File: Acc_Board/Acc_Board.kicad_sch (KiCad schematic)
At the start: 33 parts, among them J1 1053091202, J2 1053091202, J3 1053091202, J4 1053091202, J5 1053091202, J6 1053091202, K1 Relay_SPST-NO, U1 ISO1050DUB, U2 NUCLEO-L432KC, U3 L7805CV, U4 PQDE6W-Q110-S5-H-D

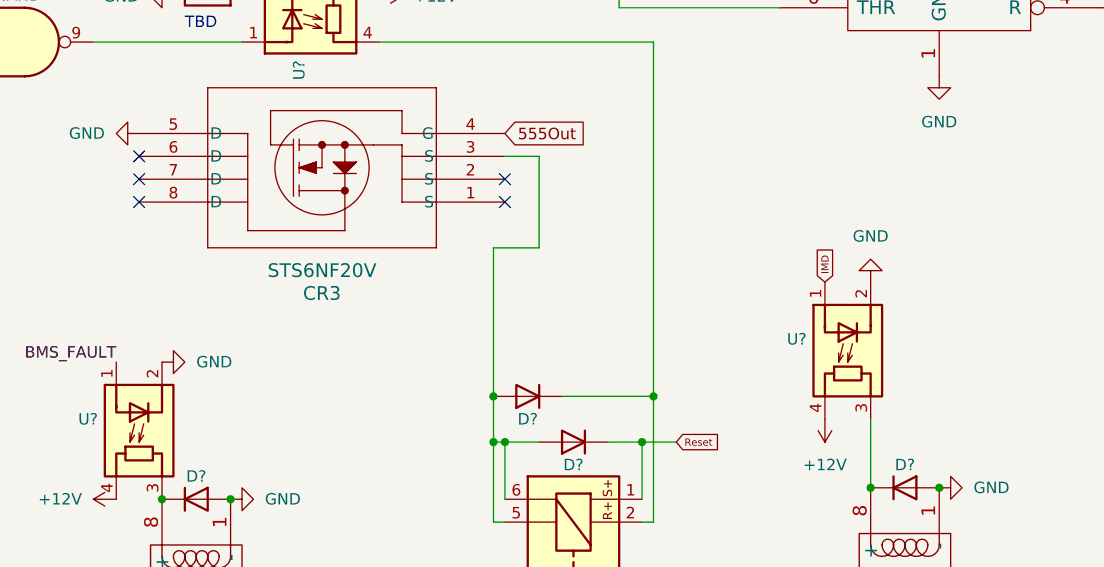
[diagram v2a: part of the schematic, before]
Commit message: Added resistors to optocouplers on ACC board
@goob10000 still needs to determine resistance
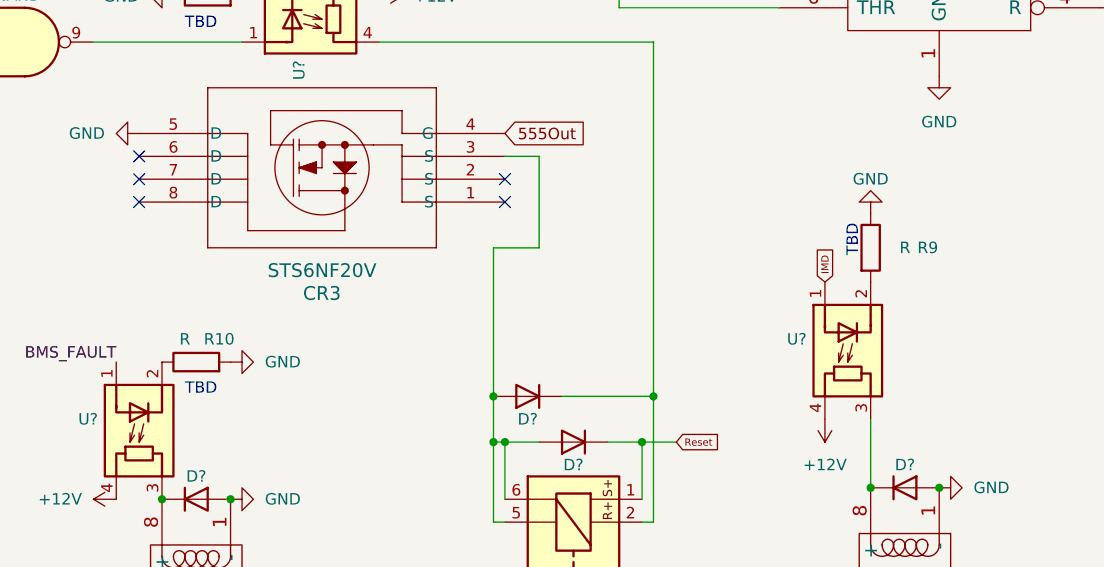
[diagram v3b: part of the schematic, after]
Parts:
- added R10, R9: R, symbol Device:R
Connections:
- net GND: now also R10.2, R9.1; no longer U?.2 (K), U?.2 (K)
- new net: R10.1, U?.2 (K)
- new net: R9.2, U?.2 (K)
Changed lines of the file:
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@@
     (effects (font (size 1.27 1.27)) (justify left bottom))
+  )
+  (text "TBD" (at 342.9 146.05 90)
+    (effects (font (size 1.27 1.27)) (justify right bottom))
   )
   (text "make cap smaller, resistor bigger\ncheck if 5V works; connect to DCDC"
@@
   )
   (text "Precharge Circuit" (at 27.94 118.11 0)
+    (effects (font (size 1.27 1.27)) (justify left bottom))
+  )
+  (text "TBD" (at 267.97 165.1 0)
     (effects (font (size 1.27 1.27)) (justify left bottom))
   )
@@
     )
   )
-  (symbol (lib_id "power:GND") (at 265.43 161.29 90) (unit 1)
-    (in_bom yes) (on_board yes) (dnp no) (fields_autoplaced)
-    (property "Reference" "#PWR016" (at 271.78 161.29 0)
-      (effects (font (size 1.27 1.27)) hide)
-    )
-    (property "Value" "GND" (at 269.24 161.29 90)
+  (symbol (lib_id "power:GND") (at 273.05 161.29 90) (unit 1)
+    (in_bom yes) (on_board yes) (dnp no)
+    (property "Reference" "#PWR016" (at 279.4 161.29 0)
+      (effects (font (size 1.27 1.27)) hide)
+    )
+    (property "Value" "GND" (at 276.86 161.29 90)
       (effects (font (size 1.27 1.27)) (justify right))
     )
-    (property "Footprint" "" (at 265.43 161.29 0)
-      (effects (font (size 1.27 1.27)) hide)
-    )
-    (property "Datasheet" "" (at 265.43 161.29 0)
+    (property "Footprint" "" (at 273.05 161.29 0)
+      (effects (font (size 1.27 1.27)) hide)
+    )
+    (property "Datasheet" "" (at 273.05 161.29 0)
       (effects (font (size 1.27 1.27)) hide)
     )
@@
         (path "/ebbe473b-926f-45d4-8349-621c37aa98bc"
           (reference "J?") (unit 1)
+        )
+      )
+    )
+  )
+  (symbol (lib_name "R_1") (lib_id "Device:R") (at 344.17 148.59 0) (unit 1)
+    (in_bom yes) (on_board yes) (dnp no)
+    (property "Reference" "R9" (at 350.52 148.59 0)
+      (effects (font (size 1.27 1.27)))
+    )
+    (property "Value" "R" (at 347.98 148.59 0)
+      (effects (font (size 1.27 1.27)))
+    )
+    (property "Footprint" "" (at 342.392 148.59 90)
+      (effects (font (size 1.27 1.27)) hide)
+    )
+    (property "Datasheet" "~" (at 344.17 148.59 0)
+      (effects (font (size 1.27 1.27)) hide)
+    )
+    (pin "1")
+    (pin "2")
+    (instances
+      (project "Acc_Board"
+        (path "/e19d26dd-723b-45e6-9d59-b1730158e759"
+          (reference "R9") (unit 1)
+        )
+      )
+    )
+  )
+  (symbol (lib_name "R_1") (lib_id "Device:R") (at 269.24 161.29 90) (unit 1)
+    (in_bom yes) (on_board yes) (dnp no)
+    (property "Reference" "R10" (at 271.78 158.75 90)
+      (effects (font (size 1.27 1.27)))
+    )
+    (property "Value" "R" (at 267.97 158.75 90)
+      (effects (font (size 1.27 1.27)))
+    )
+    (property "Footprint" "" (at 269.24 163.068 90)
+      (effects (font (size 1.27 1.27)) hide)
+    )
+    (property "Datasheet" "~" (at 269.24 161.29 0)
+      (effects (font (size 1.27 1.27)) hide)
+    )
+    (pin "1")
+    (pin "2")
+    (instances
+      (project "Acc_Board"
+        (path "/e19d26dd-723b-45e6-9d59-b1730158e759"
+          (reference "R10") (unit 1)
         )
       )
@@
     )
   )
-  (symbol (lib_id "power:GND") (at 344.17 152.4 180) (unit 1)
-    (in_bom yes) (on_board yes) (dnp no) (fields_autoplaced)
-    (property "Reference" "#PWR022" (at 344.17 146.05 0)
-      (effects (font (size 1.27 1.27)) hide)
-    )
-    (property "Value" "GND" (at 344.17 147.32 0)
-      (effects (font (size 1.27 1.27)))
-    )
-    (property "Footprint" "" (at 344.17 152.4 0)
-      (effects (font (size 1.27 1.27)) hide)
-    )
-    (property "Datasheet" "" (at 344.17 152.4 0)
-      (effects (font (size 1.27 1.27)) hide)
-    )
+  (symbol (lib_id "power:GND") (at 344.17 144.78 180) (unit 1)
+    (in_bom yes) (on_board yes) (dnp no)
+    (property "Reference" "#PWR022" (at 344.17 138.43 0)
+      (effects (font (size 1.27 1.27)) hide)
+    )
+    (property "Value" "GND" (at 344.17 140.97 0)
+      (effects (font (size 1.27 1.27)))
+    )
+    (property "Footprint" "" (at 344.17 144.78 0)
+      (effects (font (size 1.27 1.27)) hide)
+    )
+    (property "Datasheet" "" (at 344.17 144.78 0)
+      (effects (font (size 1.27 1.27)) hide)
+    )

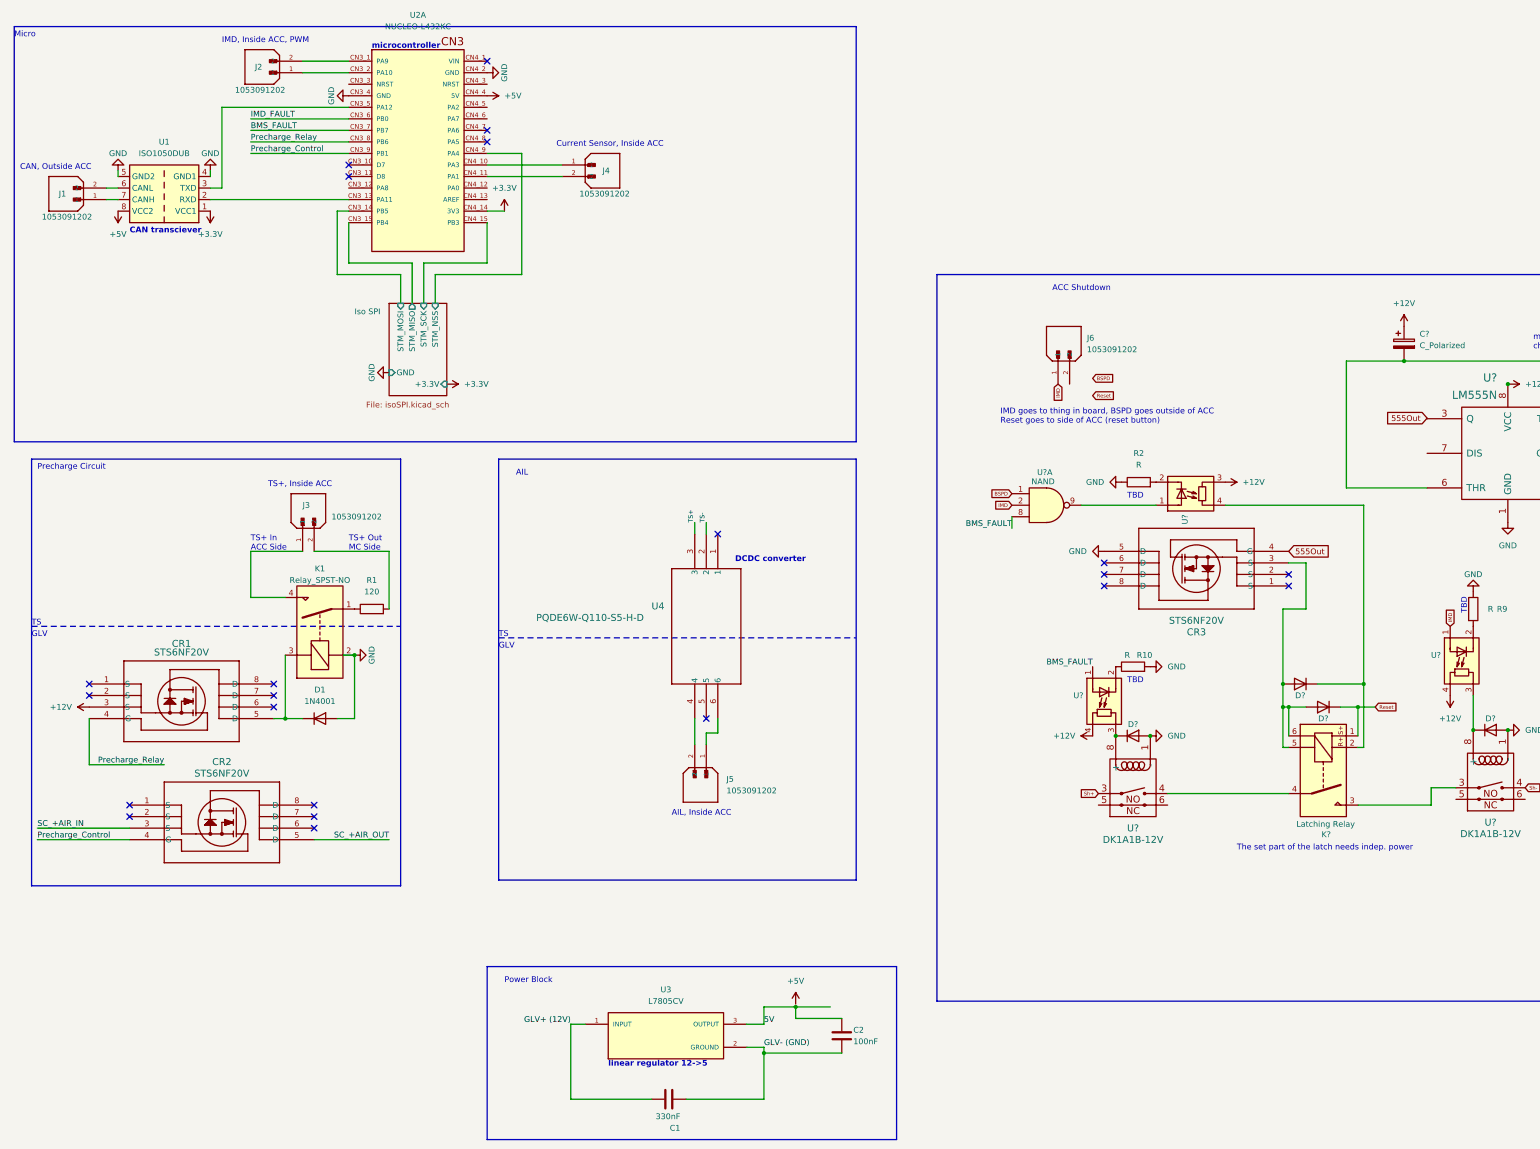
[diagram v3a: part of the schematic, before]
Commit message: Added most footprints to ACC board
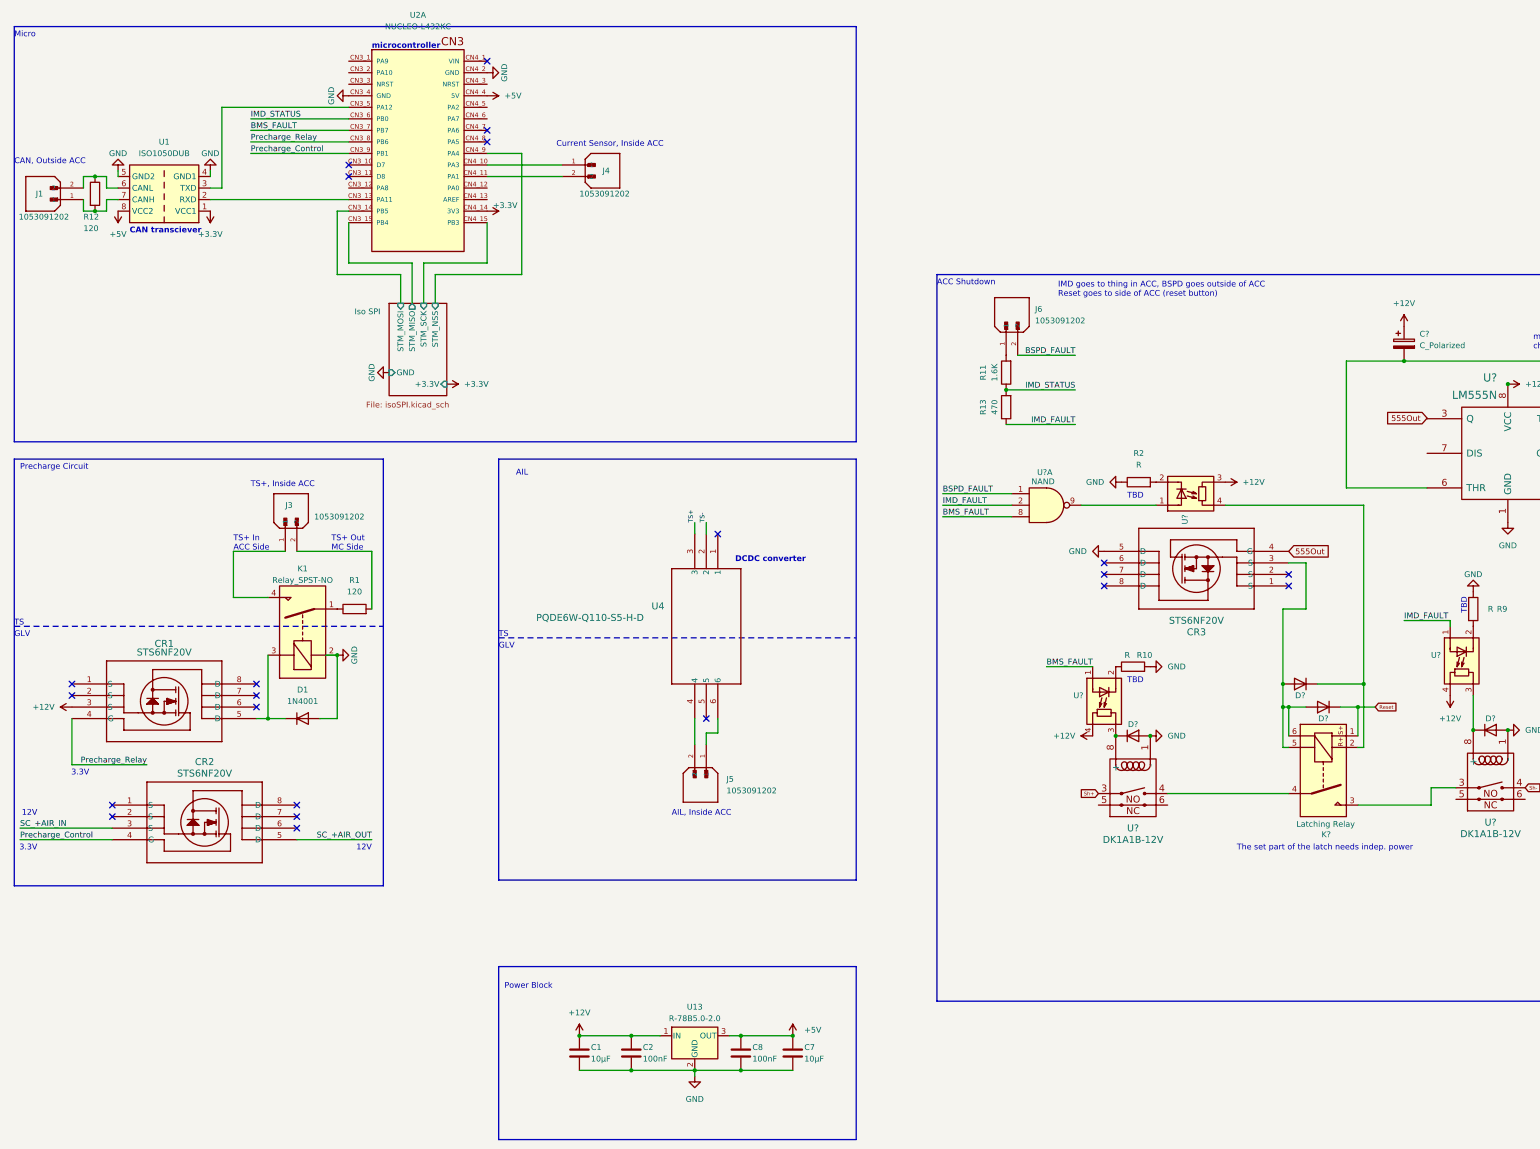
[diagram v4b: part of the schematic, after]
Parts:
- removed J2: 1053091202, 1FS_2_Global_Footprint_Library:MOLEX_1053091202, symbol molex_1053091202:1053091202
- removed U3: L7805CV, 1FS_2_Global_Footprint_Library:TO255P1040X460X1968-3, symbol 1_ACC_BOARD:L7805CV
- added C7: 10µF, Capacitor_SMD:C_0805_2012Metric_Pad1.18x1.45mm_HandSolder, symbol Device:C
- added C8: 100nF, Capacitor_SMD:C_0805_2012Metric_Pad1.18x1.45mm_HandSolder, symbol Device:C
- added R11: 1.6K, Resistor_SMD:R_0805_2012Metric_Pad1.20x1.40mm_HandSolder, symbol Device:R
- added R12: 120, Resistor_SMD:R_0805_2012Metric_Pad1.20x1.40mm_HandSolder, symbol Device:R
- added R13: 470, Resistor_SMD:R_0805_2012Metric_Pad1.20x1.40mm_HandSolder, symbol Device:R
- added U13: R-78B5.0-2.0, Converter_DCDC:Converter_DCDC_RECOM_R-78B-2.0_THT, symbol Regulator_Switching:R-78B5.0-2.0
- C1: value 330nF -> 10µF; footprint 1FS_2_Global_Footprint_Library:Basic 2 Hole -> Capacitor_SMD:C_0805_2012Metric_Pad1.18x1.45mm_HandSolder
- C2: footprint 1FS_2_Global_Footprint_Library:Basic 2 Hole -> Capacitor_SMD:C_0805_2012Metric_Pad1.18x1.45mm_HandSolder
- R10, R2, R9: footprint (none) -> Resistor_SMD:R_0805_2012Metric_Pad1.20x1.40mm_HandSolder
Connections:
- net 5V is gone; now on net GND: C2.2
- net BSPD is gone; now on net BSPD_FAULT: U?.1
- net GLV+ (12V) is gone; now on net GND: C1.2
- net GLV- (GND) is gone; now on net +12V: C1.1, C2.1
- net +12V: now also U13.1 (IN)
- net +5V: now also C7.1, C8.1, U13.3 (OUT)
- net GND: now also C7.2, C8.2, U13.2 (GND)
- net IMD_FAULT: now also U?.1 (A), U?.2, R13.1; no longer U2.CN3_6 (PB0)
- net BSPD_FAULT: now reaches J6.2
- net at J1.2, U1.6 (CANL): now also R12.1
- net at J1.1, U1.7 (CANH): now also R12.2
- removed net IMD: J6.1, U?.1 (A), U?.2
- new net: J6.1, R11.2
- new net IMD_STATUS: R11.1, R13.2, U2.CN3_6 (PB0)
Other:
- note added: "12V"
- note added: "3.3V"
- note added: "IMD goes to thing in ACC, BSPD goes outside of ACC Reset goes to side of ACC (reset button)"
- note removed: "IMD goes to thing in board, BSPD goes outside of ACC Reset goes to side of ACC (reset button)"
- note removed: "IMD, Inside ACC, PWM"
- note removed: "linear regulator 12->5"
- moved on the sheet: CR1, CR2, D1, J1, J3, J6, K1, R1
